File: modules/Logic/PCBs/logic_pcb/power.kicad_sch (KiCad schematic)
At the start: 17 parts, among them J13 Eurorack_2x8_Power, U1 CD74HCT132E, U2 CD74HCT132E, U3 LM324, U4 LM324, U5 TL072

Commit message: Switch ALU to SMD components
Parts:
- C10, C11, C12, C13, C14, C15, C8, C9: footprint Capacitor_THT:C_Disc_D4.7mm_W2.5mm_P5.00mm -> Capacitor_SMD:C_0805_2012Metric_Pad1.18x1.45mm_HandSolder; JLC (none) -> C29926
- C5, C6, C7: footprint Capacitor_THT:CP_Radial_D4.0mm_P1.50mm -> Capacitor_SMD:CP_Elec_4x5.4; JLC (none) -> C3343
- U1, U2: footprint Package_DIP:DIP-14_W7.62mm -> Package_SO:SOIC-14_3.9x8.7mm_P1.27mm; JLC (none) -> C484714
- U3, U4: footprint Package_DIP:DIP-14_W7.62mm -> Package_SO:SOIC-14_3.9x8.7mm_P1.27mm; JLC (none) -> C7943
- U5: footprint Package_DIP:DIP-8_W7.62mm -> Package_SO:SOP-8_3.9x4.9mm_P1.27mm; JLC (none) -> C5310783
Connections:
- net -12V: now reaches C12.2, C15.2, C6.2, C9.2, J13.1 (-12v), J13.2 (-12v), U3.11 (V-), U4.11 (V-), U5.4 (V-)
- net +12V: now reaches C11.1, C14.1, C5.1, C8.1, J13.10 (+12v), J13.9 (+12v), U3.4 (V+), U4.4 (V+), U5.8 (V+)
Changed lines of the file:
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@@
+	)
+	(junction
+		(at 198.12 104.14)
+		(diameter 0)
+		(color 0 0 0 0)
 	)
 	(junction
@@
 	)
 	(junction
+		(at 198.12 88.9)
+		(diameter 0)
+		(color 0 0 0 0)
+	)
+	(junction
 		(at 138.43 96.52)
 		(diameter 0)
@@
 	(wire
 		(pts
+			(xy 200.66 104.14) (xy 198.12 104.14)
+		)
+		(stroke
+			(width 0)
+			(type default)
+		)
+	)
+	(wire
+		(pts
 			(xy 158.75 85.09) (xy 146.05 85.09)
 		)
@@
 	(wire
 		(pts
+			(xy 198.12 88.9) (xy 200.66 88.9)
+		)
+		(stroke
+			(width 0)
+			(type default)
+		)
+	)
+	(wire
+		(pts
 			(xy 146.05 85.09) (xy 146.05 67.31)
 		)
@@
 			(width 0)
 			(type default)
+		)
+	)
+	(label "-12V"
+		(at 200.66 104.14 0)
+		(effects
+			(font
+				(size 1.27 1.27)
+			)
+			(justify left bottom)
+		)
+	)
+	(label "+12V"
+		(at 200.66 88.9 0)
+		(effects
+			(font
+				(size 1.27 1.27)
+			)
+			(justify left bottom)
 		)
 	)
@@
 		(shape output)
 		(at 187.96 85.09 0)
-		(fields_autoplaced yes)
 		(effects
 			(font
@@
 		(shape output)
 		(at 187.96 59.69 0)
-		(fields_autoplaced yes)
 		(effects
 			(font
@@
 			)
 		)
+		(property "JLC" ""
+			(at 92.71 93.98 0)
+			(effects
+				(font
+					(size 1.27 1.27)
+				)
+				(hide yes)
+			)
+		)
 		(pin "7"
 		)
@@
 			)
 		)
-		(property "Footprint" "Capacitor_THT:C_Disc_D4.7mm_W2.5mm_P5.00mm"
+		(property "Footprint" "Capacitor_SMD:C_0805_2012Metric_Pad1.18x1.45mm_HandSolder"
 			(at 153.3652 104.14 0)
 			(effects
@@
 		)
 		(property "Description" "Unpolarized capacitor"
+			(at 152.4 100.33 0)
+			(effects
+				(font
+					(size 1.27 1.27)
+				)
+				(hide yes)
+			)
+		)
+		(property "JLC" "C29926"
 			(at 152.4 100.33 0)
 			(effects
@@
 			)
 		)
-		(property "Footprint" "Package_DIP:DIP-14_W7.62mm"
+		(property "Footprint" "Package_SO:SOIC-14_3.9x8.7mm_P1.27mm"
 			(at 158.75 72.39 0)
 			(effects
@@
 		)
 		(property "Description" "quad 2-input NAND gate"
+			(at 158.75 72.39 0)
+			(effects
+				(font
+					(size 1.27 1.27)
+				)
+				(hide yes)
+			)
+		)
+		(property "JLC" "C484714"
 			(at 158.75 72.39 0)
 			(effects
@@
 			)
 		)
-		(property "Footprint" "Capacitor_THT:CP_Radial_D4.0mm_P1.50mm"
+		(property "Footprint" "Capacitor_SMD:CP_Elec_4x5.4"
 			(at 111.76 100.33 0)
 			(effects
@@
 		)
 		(property "Description" "Polarized capacitor, US symbol"
+			(at 111.76 100.33 0)
+			(effects
+				(font
+					(size 1.27 1.27)
+				)
+				(hide yes)
+			)
+		)
+		(property "JLC" "C3343"
 			(at 111.76 100.33 0)
 			(effects
@@
 			)
 		)
-		(property "Footprint" "Capacitor_THT:CP_Radial_D4.0mm_P1.50mm"
+		(property "Footprint" "Capacitor_SMD:CP_Elec_4x5.4"
 			(at 111.76 92.71 0)
 			(effects
@@
 		)
 		(property "Description" "Polarized capacitor, US symbol"
+			(at 111.76 92.71 0)
+			(effects
+				(font
+					(size 1.27 1.27)
+				)
+				(hide yes)
+			)
+		)
+		(property "JLC" "C3343"
 			(at 111.76 92.71 0)
 			(effects
@@
 			)
 		)
-		(property "Footprint" "Capacitor_THT:C_Disc_D4.7mm_W2.5mm_P5.00mm"
+		(property "Footprint" "Capacitor_SMD:C_0805_2012Metric_Pad1.18x1.45mm_HandSolder"
 			(at 139.3952 104.14 0)
 			(effects
@@
 		)
 		(property "Description" "Unpolarized capacitor"
+			(at 138.43 100.33 0)
+			(effects
+				(font
+					(size 1.27 1.27)
+				)
+				(hide yes)
+			)
+		)
+		(property "JLC" "C29926"
 			(at 138.43 100.33 0)
 			(effects
@@
 			)
 		)
-		(property "Footprint" "Capacitor_THT:C_Disc_D4.7mm_W2.5mm_P5.00mm"
+		(property "Footprint" "Capacitor_SMD:C_0805_2012Metric_Pad1.18x1.45mm_HandSolder"
 			(at 153.3652 96.52 0)
 			(effects
@@
 		)
 		(property "Description" "Unpolarized capacitor"
+			(at 152.4 92.71 0)
+			(effects
+				(font
+					(size 1.27 1.27)
+				)
+				(hide yes)
+			)
+		)
+		(property "JLC" "C29926"
 			(at 152.4 92.71 0)
 			(effects
@@
 			)
 		)
-		(property "Footprint" "Package_DIP:DIP-8_W7.62mm"
+		(property "Footprint" "Package_SO:SOP-8_3.9x4.9mm_P1.27mm"
 			(at 200.66 96.52 0)
 			(effects
@@
 		)
 		(property "Description" "Dual Low-Noise JFET-Input Operational Amplifiers, DIP-8/SOIC-8"
+			(at 200.66 96.52 0)
+			(effects
+				(font
+					(size 1.27 1.27)
+				)
+				(hide yes)
+			)
+		)
+		(property "JLC" "C5310783"
 			(at 200.66 96.52 0)
 			(effects
@@
 			)
 		)
-		(property "Footprint" "Package_DIP:DIP-14_W7.62mm"
+		(property "Footprint" "Package_SO:SOIC-14_3.9x8.7mm_P1.27mm"
 			(at 185.42 72.39 0)
 			(effects
@@
 		)
 		(property "Description" "quad 2-input NAND gate"
+			(at 185.42 72.39 0)
+			(effects
+				(font
+					(size 1.27 1.27)
+				)
+				(hide yes)
+			)
+		)
+		(property "JLC" "C484714"
 			(at 185.42 72.39 0)
 			(effects
@@
 			)
 		)
-		(property "Footprint" "Capacitor_THT:C_Disc_D4.7mm_W2.5mm_P5.00mm"
+		(property "Footprint" "Capacitor_SMD:C_0805_2012Metric_Pad1.18x1.45mm_HandSolder"
 			(at 139.3952 96.52 0)
 			(effects
@@
 		)
 		(property "Description" "Unpolarized capacitor"
+			(at 138.43 92.71 0)
+			(effects
+				(font
+					(size 1.27 1.27)
+				)
+				(hide yes)
+			)
+		)
+		(property "JLC" "C29926"
 			(at 138.43 92.71 0)
 			(effects
@@
 			)
 		)
-		(property "Footprint" "Package_DIP:DIP-14_W7.62mm"
+		(property "Footprint" "Package_SO:SOIC-14_3.9x8.7mm_P1.27mm"
 			(at 185.42 93.98 0)
 			(effects
@@
 		)
 		(property "Description" "Low-Power, Quad-Operational Amplifiers, DIP-14/SOIC-14/SSOP-14"
+			(at 186.69 96.52 0)
+			(effects
+				(font
+					(size 1.27 1.27)
+				)
+				(hide yes)
+			)
+		)
+		(property "JLC" "C7943"
 			(at 186.69 96.52 0)
 			(effects
@@
 			)
 		)
-		(property "Footprint" "Capacitor_THT:C_Disc_D4.7mm_W2.5mm_P5.00mm"
+		(property "Footprint" "Capacitor_SMD:C_0805_2012Metric_Pad1.18x1.45mm_HandSolder"
 			(at 125.4252 96.52 0)
 			(effects
@@
 		)
 		(property "Description" "Unpolarized capacitor"
+			(at 124.46 92.71 0)
+			(effects
+				(font
+					(size 1.27 1.27)
+				)
+				(hide yes)
+			)
+		)
+		(property "JLC" "C29926"
 			(at 124.46 92.71 0)
 			(effects
@@
 			)
 		)
-		(property "Footprint" "Capacitor_THT:CP_Radial_D4.0mm_P1.50mm"
+		(property "Footprint" "Capacitor_SMD:CP_Elec_4x5.4"
 			(at 113.03 63.5 0)
 			(effects
@@
 		)
 		(property "Description" "Polarized capacitor, US symbol"
+			(at 113.03 63.5 0)
+			(effects
+				(font
+					(size 1.27 1.27)
+				)
+				(hide yes)
+			)
+		)
+		(property "JLC" "C3343"
 			(at 113.03 63.5 0)
 			(effects
@@
 			)
 		)
-		(property "Footprint" "Package_DIP:DIP-14_W7.62mm"
+		(property "Footprint" "Package_SO:SOIC-14_3.9x8.7mm_P1.27mm"
 			(at 170.18 93.98 0)
 			(effects
@@
 		)
 		(property "Description" "Low-Power, Quad-Operational Amplifiers, DIP-14/SOIC-14/SSOP-14"
+			(at 171.45 96.52 0)
+			(effects
+				(font
+					(size 1.27 1.27)
+				)
+				(hide yes)
+			)
+		)
+		(property "JLC" "C7943"
 			(at 171.45 96.52 0)
 			(effects
@@
 			)
 		)
-		(property "Footprint" "Capacitor_THT:C_Disc_D4.7mm_W2.5mm_P5.00mm"
+		(property "Footprint" "Capacitor_SMD:C_0805_2012Metric_Pad1.18x1.45mm_HandSolder"
 			(at 125.4252 104.14 0)
 			(effects
@@
 		)
 		(property "Description" "Unpolarized capacitor"
+			(at 124.46 100.33 0)
+			(effects
+				(font
+					(size 1.27 1.27)
+				)
+				(hide yes)
+			)
+		)
+		(property "JLC" "C29926"
 			(at 124.46 100.33 0)
 			(effects
@@
 			)
 		)
-		(property "Footprint" "Capacitor_THT:C_Disc_D4.7mm_W2.5mm_P5.00mm"
+		(property "Footprint" "Capacitor_SMD:C_0805_2012Metric_Pad1.18x1.45mm_HandSolder"
 			(at 141.9352 67.31 0)
 			(effects
@@
 		)
 		(property "Description" "Unpolarized capacitor"
+			(at 140.97 63.5 0)
+			(effects
+				(font
+					(size 1.27 1.27)
+				)
+				(hide yes)
+			)
+		)
+		(property "JLC" "C29926"
 			(at 140.97 63.5 0)
 			(effects
@@
 			)
 		)
-		(property "Footprint" "Capacitor_THT:C_Disc_D4.7mm_W2.5mm_P5.00mm"
+		(property "Footprint" "Capacitor_SMD:C_0805_2012Metric_Pad1.18x1.45mm_HandSolder"
 			(at 127.9652 67.31 0)
 			(effects
@@
 			(at 127 63.5 0)
 			(effects
+				(font
+					(size 1.27 1.27)
+				)
+				(hide yes)
+			)
+		)
+		(property "JLC" "C29926"
+			(at 127 63.5 0)
+			(effects

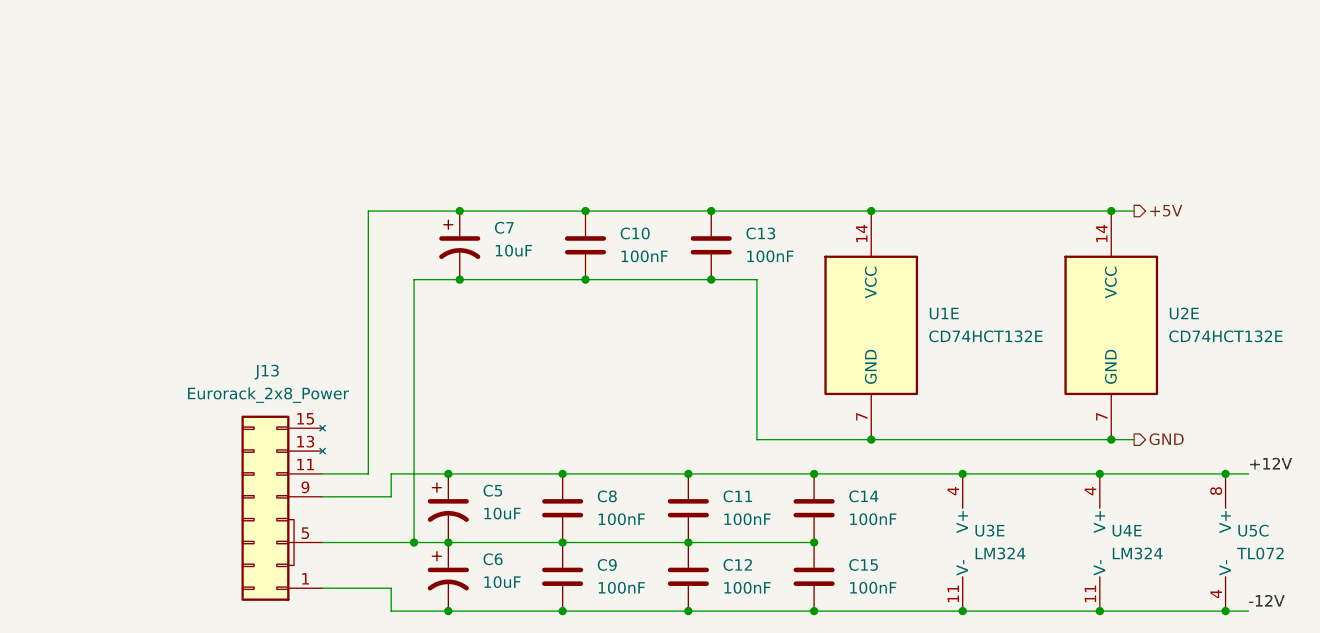
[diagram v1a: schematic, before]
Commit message: [WIP] re-layout back panel to 4hp
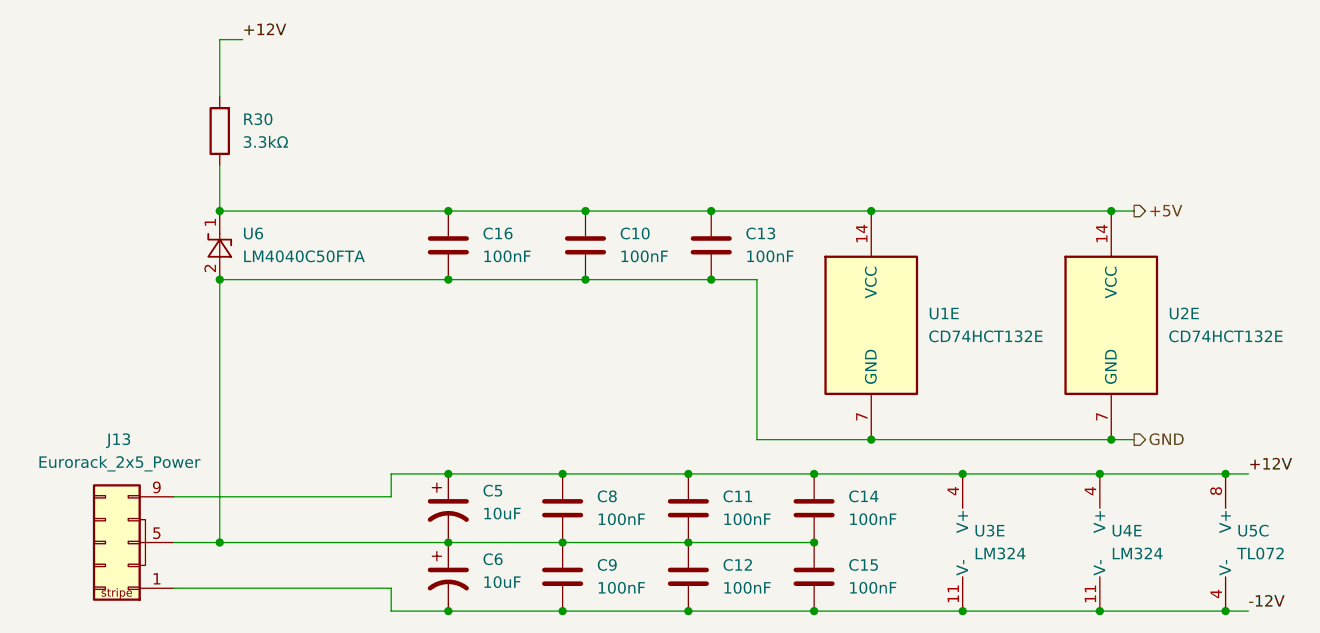
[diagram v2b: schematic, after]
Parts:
- removed C7: 10uF, Capacitor_SMD:CP_Elec_4x5.4, symbol Device:C_Polarized_US
- removed J13: Eurorack_2x8_Power, Connector_IDC:IDC-Header_2x08_P2.54mm_Vertical, symbol FreeModular:Eurorack_2x8_Power
- added C16: 100nF, Capacitor_SMD:C_0805_2012Metric_Pad1.18x1.45mm_HandSolder, symbol Device:C
- added J13: Eurorack_2x5_Power, Connector_IDC:IDC-Header_2x05_P2.54mm_Vertical, symbol FreeModular:Eurorack_2x5_Power
- added R30: 3.3kΩ, Resistor_SMD:R_0805_2012Metric_Pad1.20x1.40mm_HandSolder, symbol Device:R
- added U6: LM4040C50FTA, Package_TO_SOT_SMD:SOT-23, symbol Reference_Voltage:LM4040DBZ-5
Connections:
- net +12V: now also J13.10 (+12v), J13.9 (+12v), R30.2
- net +5V: now also C16.1, R30.1, U6.1 (K)
- net -12V: now also J13.1 (-12v), J13.2 (-12v)
- net GND: now also C16.2, J13.3 (GND), J13.4 (GND), J13.5 (GND), J13.6 (GND), J13.7 (GND), J13.8 (GND), U6.2 (A)

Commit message: Add silkscreen labels to PCB
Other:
- company: (none) -> Free Modular
- title: (none) -> ALU
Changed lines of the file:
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@@
 (kicad_sch
-	(version 20231120)
+	(version 20250114)
 	(generator "eeschema")
-	(generator_version "8.0")
+	(generator_version "9.0")
 	(paper "A4")
+	(title_block
+		(title "ALU")
+		(date "2025-04-06")
+		(rev "v0.1")
+		(company "Free Modular")
+	)
 	(junction
 		(at 124.46 96.52)

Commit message: Fix some DRC errors
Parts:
- J13: now left out of the parts list
- U6: JLC (none) -> C156291
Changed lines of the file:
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@@
+			)
+		)
+		(property "JLC" "C156291"
+			(at 86.36 63.5 90)
+			(effects
+				(font
+					(size 1.27 1.27)
+				)
+				(hide yes)
 			)
 		)
@@
 		(unit 1)
 		(exclude_from_sim no)
-		(in_bom yes)
-		(on_board yes)
-		(dnp no)
+		(in_bom no)
+		(on_board yes)
+		(dnp no)
